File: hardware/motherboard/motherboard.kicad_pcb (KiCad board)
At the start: 2 copper layers, 83.7 x 56.7 mm, 55 parts, among them J1 Conn_01x02, J2 Conn_02x03_Odd_Even, J3 Conn_01x04, U1 ESP32-WROOM-32, U2 SHTC3, U3 BMP390, U4 TPS62177DQC, U8 NRF24L01_Breakout

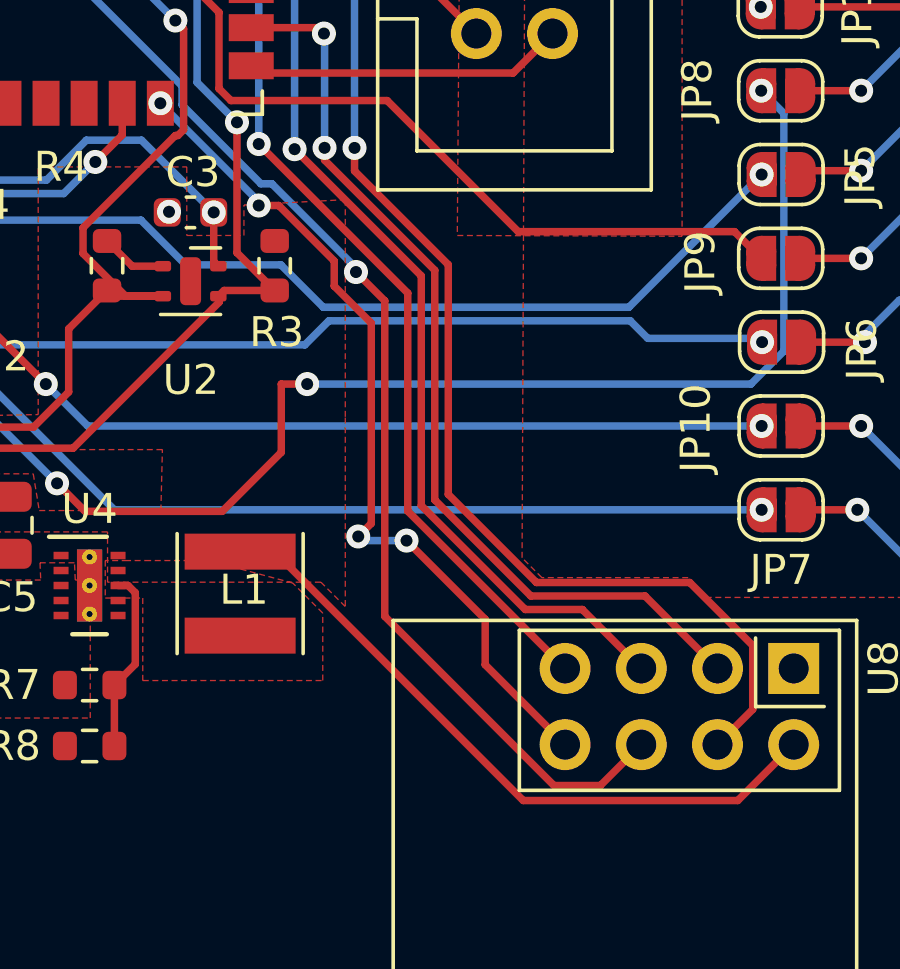
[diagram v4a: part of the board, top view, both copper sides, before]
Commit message: Removed Via bridge
rerouted one trace to remove via bridge and keep it neatly on one layer
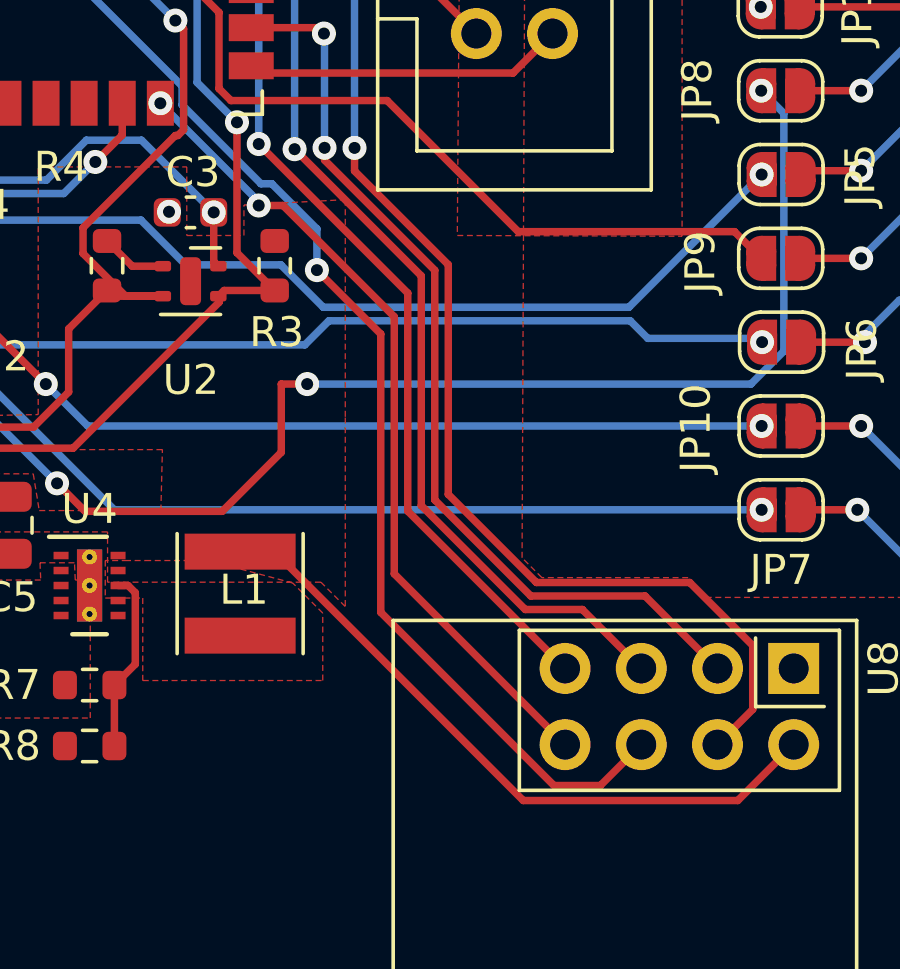
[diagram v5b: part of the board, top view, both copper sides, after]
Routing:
- net /RF_{INT}: track 28.6 -> 27.4 mm, vias 4 -> 2
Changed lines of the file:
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@@
   (via (at 201 110.525) (size 0.8) (drill 0.4) (layers "F.Cu" "B.Cu") (net 9))
   (segment (start 201 110.525) (end 201 125.325) (width 0.25) (layer "B.Cu") (net 9))
-  (segment (start 163.317254 115.843352) (end 162.357451 114.883549) (width 0.25) (layer "F.Cu") (net 10))
+  (segment (start 163.184 126.227) (end 168.957 132) (width 0.25) (layer "F.Cu") (net 10))
+  (segment (start 163.184 116.948798) (end 163.184 126.227) (width 0.25) (layer "F.Cu") (net 10))
   (segment (start 175.119 91.314) (end 170.814 91.314) (width 0.25) (layer "F.Cu") (net 10))
   (segment (start 160.72273 92.767874) (end 158.8668 92.767874) (width 0.25) (layer "F.Cu") (net 10))
-  (segment (start 163.317254 126.360254) (end 163.317254 115.843352) (width 0.25) (layer "F.Cu") (net 10))
-  (segment (start 170.505 132) (end 168.957 132) (width 0.25) (layer "F.Cu") (net 10))
-  (segment (start 171.868 130.637) (end 170.505 132) (width 0.25) (layer "F.Cu") (net 10))
+  (segment (start 170.505 132) (end 171.868 130.637) (width 0.25) (layer "F.Cu") (net 10))
+  (segment (start 168.957 132) (end 170.505 132) (width 0.25) (layer "F.Cu") (net 10))
   (segment (start 170.814 91.314) (end 170.25 90.75) (width 0.25) (layer "F.Cu") (net 10))
   (segment (start 170.25 90.75) (end 162.740604 90.75) (width 0.25) (layer "F.Cu") (net 10))
+  (segment (start 161.055101 114.819899) (end 163.184 116.948798) (width 0.25) (layer "F.Cu") (net 10))
   (segment (start 175.88 92.075) (end 175.119 91.314) (width 0.25) (layer "F.Cu") (net 10))
   (segment (start 162.740604 90.75) (end 160.72273 92.767874) (width 0.25) (layer "F.Cu") (net 10))
-  (segment (start 168.957 132) (end 163.317254 126.360254) (width 0.25) (layer "F.Cu") (net 10))
   (via (at 158.8668 92.767874) (size 0.8) (drill 0.4) (layers "F.Cu" "B.Cu") (net 10))
-  (via (at 162.357451 114.883549) (size 0.8) (drill 0.4) (layers "F.Cu" "B.Cu") (net 10))
+  (via (at 161.055101 114.819899) (size 0.8) (drill 0.4) (layers "F.Cu" "B.Cu") (net 10))
+  (segment (start 156.5618 109.3118) (end 156.5618 108.6828) (width 0.25) (layer "B.Cu") (net 10))
+  (segment (start 157.982126 92.767874) (end 158.8668 92.767874) (width 0.25) (layer "B.Cu") (net 10))
+  (segment (start 156.5618 108.6828) (end 153 105.121) (width 0.25) (layer "B.Cu") (net 10))
+  (segment (start 159.552645 111.940694) (end 159.190694 111.940694) (width 0.25) (layer "B.Cu") (net 10))
+  (segment (start 161.055101 113.44315) (end 159.552645 111.940694) (width 0.25) (layer "B.Cu") (net 10))
+  (segment (start 161.055101 114.819899) (end 161.055101 113.44315) (width 0.25) (layer "B.Cu") (net 10))
+  (segment (start 153 105.121) (end 153 97.75) (width 0.25) (layer "B.Cu") (net 10))
   (segment (start 153 97.75) (end 157.982126 92.767874) (width 0.25) (layer "B.Cu") (net 10))
   (segment (start 159.190694 111.940694) (end 156.5618 109.3118) (width 0.25) (layer "B.Cu") (net 10))
-  (segment (start 156.5618 109.3118) (end 156.5618 108.6828) (width 0.25) (layer "B.Cu") (net 10))
-  (segment (start 159.552645 111.940694) (end 159.190694 111.940694) (width 0.25) (layer "B.Cu") (net 10))
-  (segment (start 162.357451 114.883549) (end 162.357451 114.7455) (width 0.25) (layer "B.Cu") (net 10))
-  (segment (start 153 105.121) (end 153 97.75) (width 0.25) (layer "B.Cu") (net 10))
-  (segment (start 162.357451 114.7455) (end 159.552645 111.940694) (width 0.25) (layer "B.Cu") (net 10))
-  (segment (start 157.982126 92.767874) (end 158.8668 92.767874) (width 0.25) (layer "B.Cu") (net 10))
-  (segment (start 156.5618 108.6828) (end 153 105.121) (width 0.25) (layer "B.Cu") (net 10))
   (segment (start 198.814 101.99162) (end 198.814 105.05162) (width 0.25) (layer "F.Cu") (net 11))
   (segment (start 198.814 105.05162) (end 195.713 108.15262) (width 0.25) (layer "F.Cu") (net 11))
@@
   (segment (start 153.67 111.2145) (end 152.6165 112.268) (width 0.25) (layer "B.Cu") (net 41))
   (segment (start 152.6165 112.268) (end 148.1165 112.268) (width 0.25) (layer "B.Cu") (net 41))
-  (segment (start 169.328 130.637) (end 166.664802 127.973802) (width 0.25) (layer "F.Cu") (net 42))
-  (segment (start 161.632451 114.515451) (end 159.782694 112.665694) (width 0.25) (layer "F.Cu") (net 42))
-  (segment (start 159.782694 112.665694) (end 159.1155 112.665694) (width 0.25) (layer "F.Cu") (net 42))
-  (segment (start 162.867254 123.263746) (end 162.867254 116.586) (width 0.25) (layer "F.Cu") (net 42))
-  (segment (start 161.632451 115.351197) (end 161.632451 114.515451) (width 0.25) (layer "F.Cu") (net 42))
-  (segment (start 166.664802 126.4584) (end 164.042254 123.835852) (width 0.25) (layer "F.Cu") (net 42))
-  (segment (start 162.867254 116.586) (end 161.632451 115.351197) (width 0.25) (layer "F.Cu") (net 42))
-  (segment (start 162.433 123.698) (end 162.867254 123.263746) (width 0.25) (layer "F.Cu") (net 42))
-  (segment (start 166.664802 127.973802) (end 166.664802 126.4584) (width 0.25) (layer "F.Cu") (net 42))
+  (segment (start 163.634 116.373493) (end 163.634 124.943) (width 0.25) (layer "F.Cu") (net 42))
+  (segment (start 159.926201 112.665694) (end 163.634 116.373493) (width 0.25) (layer "F.Cu") (net 42))
+  (segment (start 159.1155 112.665694) (end 159.926201 112.665694) (width 0.25) (layer "F.Cu") (net 42))
+  (segment (start 163.634 124.943) (end 169.328 130.637) (width 0.25) (layer "F.Cu") (net 42))
   (via (at 159.1155 112.665694) (size 0.8) (drill 0.4) (layers "F.Cu" "B.Cu") (net 42))
-  (via (at 164.042254 123.835852) (size 0.8) (drill 0.4) (layers "F.Cu" "B.Cu") (net 42))
   (via (at 155.8368 109.257874) (size 0.8) (drill 0.4) (layers "F.Cu" "B.Cu") (net 42))
-  (via (at 162.433 123.698) (size 0.8) (drill 0.4) (layers "F.Cu" "B.Cu") (net 42))
-  (segment (start 164.042254 123.835852) (end 162.570852 123.835852) (width 0.25) (layer "B.Cu") (net 42))
-  (segment (start 162.570852 123.835852) (end 162.433 123.698) (width 0.25) (layer "B.Cu") (net 42))
   (segment (start 159.1155 112.665694) (end 159.1155 112.536574) (width 0.25) (layer "B.Cu") (net 42))
   (segment (start 159.1155 112.536574) (end 155.8368 109.257874) (width 0.25) (layer "B.Cu") (net 42))

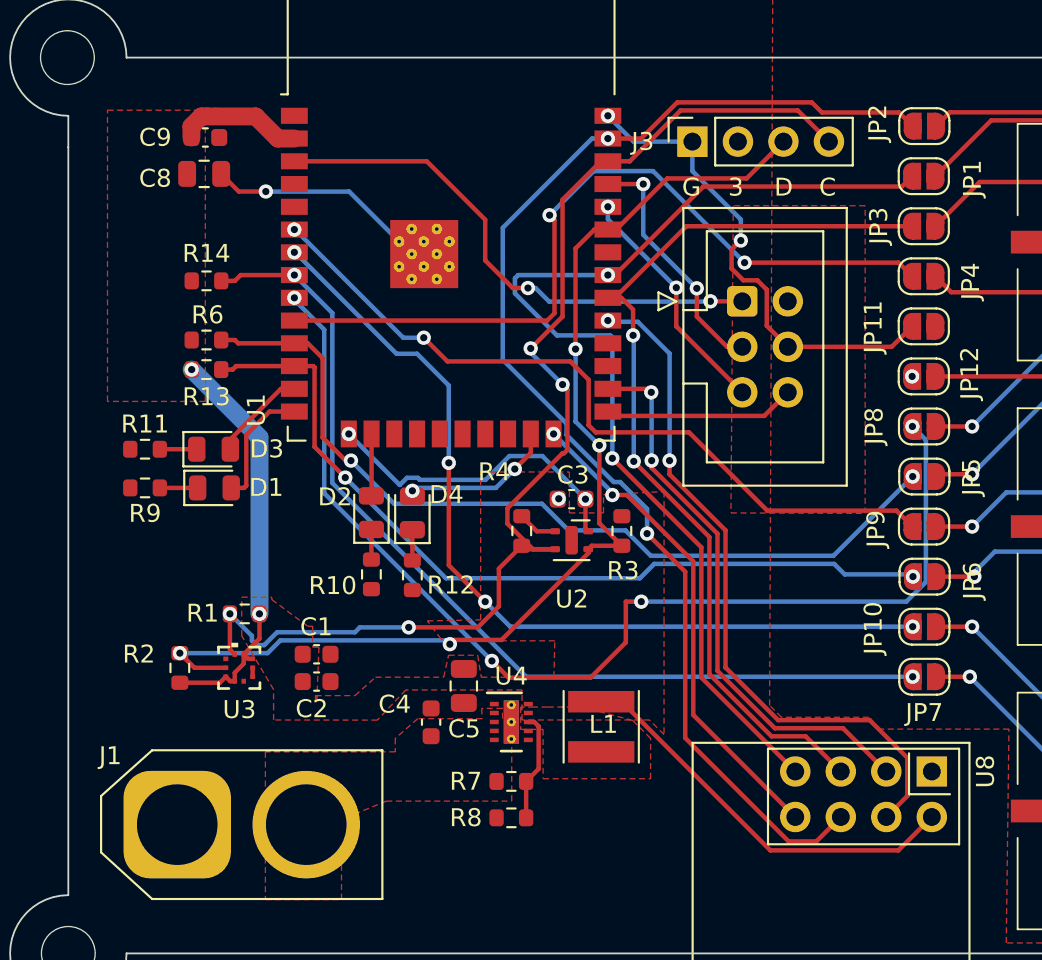
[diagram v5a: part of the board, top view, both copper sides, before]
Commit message: Simpler power routing
Added vias to connect power to flood on back layer rather than running traces on top layer
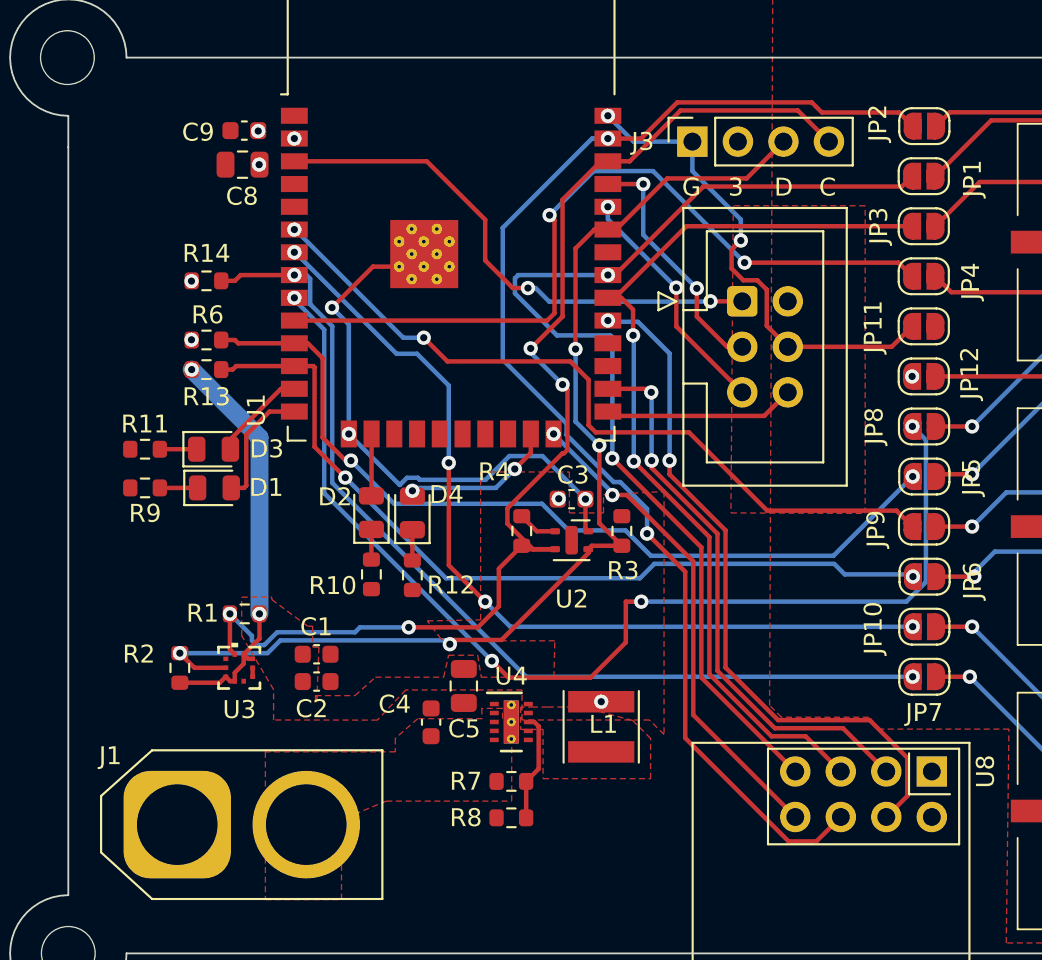
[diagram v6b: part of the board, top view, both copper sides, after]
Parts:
- moved C9 2.21 mm to (138.6, 92.3), turned to 0 degrees
- moved C8 2.20 mm to (138.5, 94.2), turned to 0 degrees
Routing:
- net +3.3V: track 55.8 -> 26.2 mm, vias 4 -> 10
- net GND: track 58.8 -> 63.4 mm

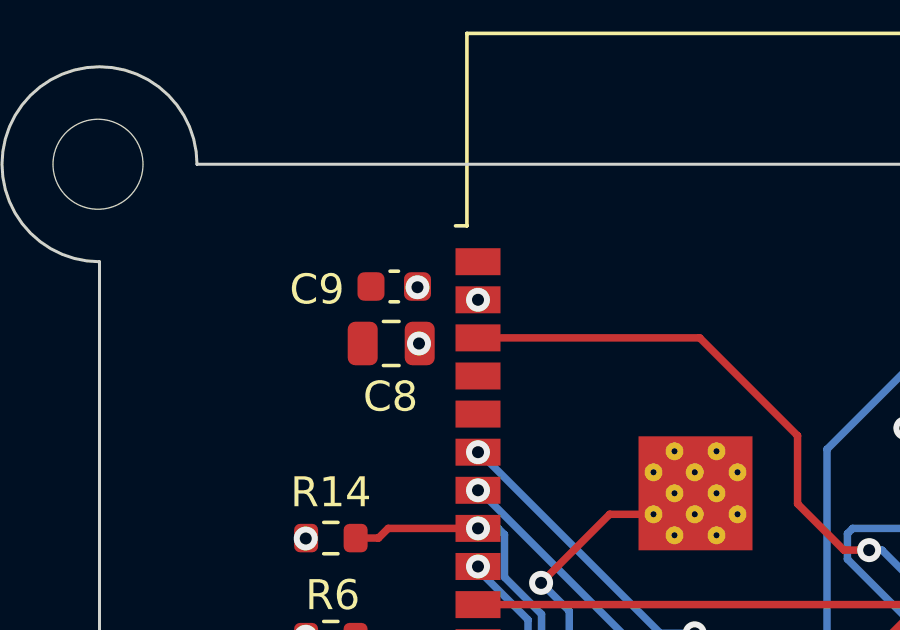
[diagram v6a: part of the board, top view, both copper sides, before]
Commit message: Fixed Decoupling Capaciors for ESP32
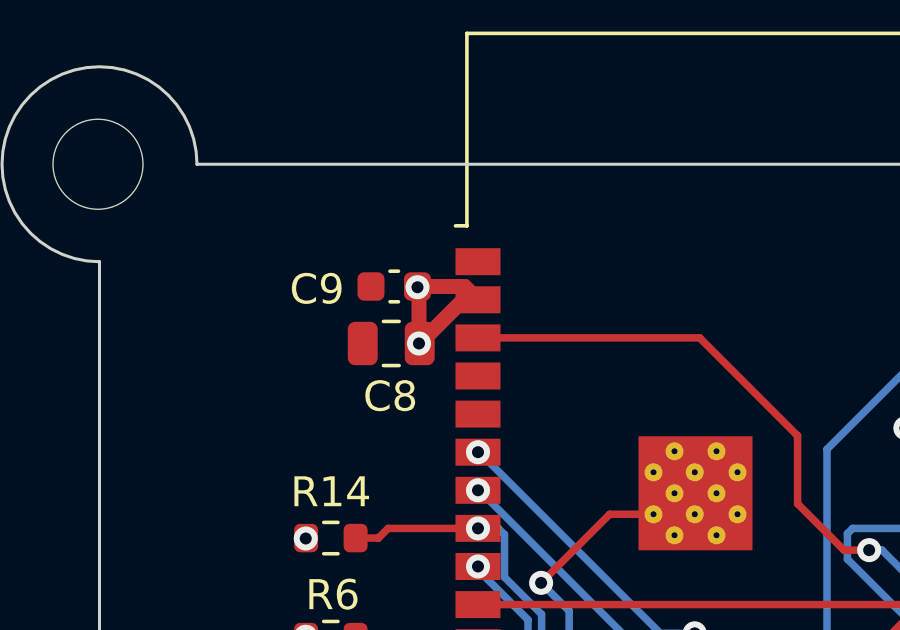
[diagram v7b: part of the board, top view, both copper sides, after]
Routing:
- net +3.3V: track 26.2 -> 32.9 mm, vias 10 -> 9
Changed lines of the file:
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@@
   (segment (start 154.405114 101.112374) (end 154.833374 101.112374) (width 0.25) (layer "B.Cu") (net 2))
   (segment (start 164.575503 101.870497) (end 164.592 101.854) (width 0.25) (layer "B.Cu") (net 2))
+  (segment (start 139.4 92.4) (end 139.35 92.35) (width 0.25) (layer "F.Cu") (net 3))
   (segment (start 159.695 113.848) (end 159.766 113.919) (width 0.25) (layer "F.Cu") (net 3))
   (segment (start 134.9756 123.141748) (end 137.208252 123.141748) (width 0.25) (layer "F.Cu") (net 3))
+  (segment (start 140.923926 92.325) (end 141.3668 92.767874) (width 0.5) (layer "F.Cu") (net 3))
   (segment (start 135.637 100.711) (end 135.614 100.711) (width 0.25) (layer "F.Cu") (net 3))
   (segment (start 138.040237 122.581917) (end 138.040237 123.058174) (width 0.25) (layer "F.Cu") (net 3))
@@
   (segment (start 138.040237 123.058174) (end 137.790174 123.058174) (width 0.25) (layer "F.Cu") (net 3))
   (segment (start 138.540363 121.559574) (end 138.540363 122.081791) (width 0.25) (layer "F.Cu") (net 3))
+  (segment (start 139.35 92.325) (end 140.923926 92.325) (width 0.5) (layer "F.Cu") (net 3))
   (segment (start 156.105 112.895) (end 156.125 112.875) (width 0.25) (layer "F.Cu") (net 3))
   (segment (start 135.614 100.711) (end 135.6 100.725) (width 0.25) (layer "F.Cu") (net 3))
@@
   (segment (start 137.208252 123.141748) (end 137.541 122.809) (width 0.25) (layer "F.Cu") (net 3))
   (segment (start 156.066 112.895) (end 156.105 112.895) (width 0.25) (layer "F.Cu") (net 3))
+  (segment (start 140.882126 92.767874) (end 141.3668 92.767874) (width 0.5) (layer "F.Cu") (net 3))
   (segment (start 139.0396 121.808748) (end 138.789537 121.808748) (width 0.25) (layer "F.Cu") (net 3))
+  (segment (start 139.425 94.225) (end 140.882126 92.767874) (width 0.5) (layer "F.Cu") (net 3))
   (segment (start 158.366 124.333) (end 158.496 124.203) (width 0.25) (layer "F.Cu") (net 3))
   (segment (start 139.4196 119.298748) (end 139.4196 120.680337) (width 0.25) (layer "F.Cu") (net 3))
+  (segment (start 139.4 94.225) (end 139.4 92.4) (width 0.5) (layer "F.Cu") (net 3))
   (via (at 135.636 105.664) (size 0.8) (drill 0.4) (layers "F.Cu" "B.Cu") (net 3))
   (via (at 175.85 106.045) (size 0.8) (drill 0.4) (layers "F.Cu" "B.Cu") (net 3))
-  (via (at 141.3668 92.767874) (size 0.8) (drill 0.4) (layers "F.Cu" "B.Cu") (net 3))
   (via (at 156.125 112.875) (size 0.8) (drill 0.4) (layers "F.Cu" "B.Cu") (net 3))
   (via (at 158.496 124.203) (size 0.8) (drill 0.4) (layers "F.Cu" "B.Cu") (net 3))
